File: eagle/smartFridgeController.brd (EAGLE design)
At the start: 35.9 x 41.9 mm, 13 parts

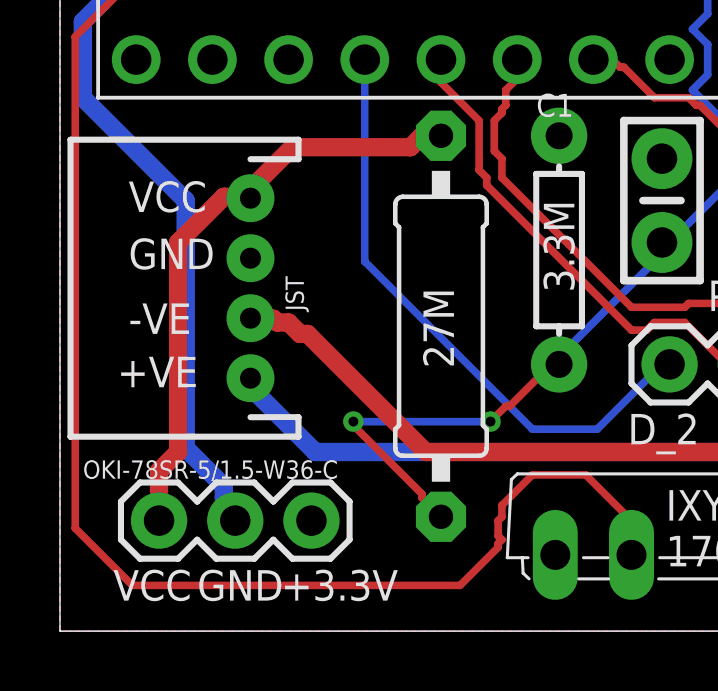
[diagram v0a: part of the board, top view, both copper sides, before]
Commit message: gnd, vcc switch, labled switch on oki-78
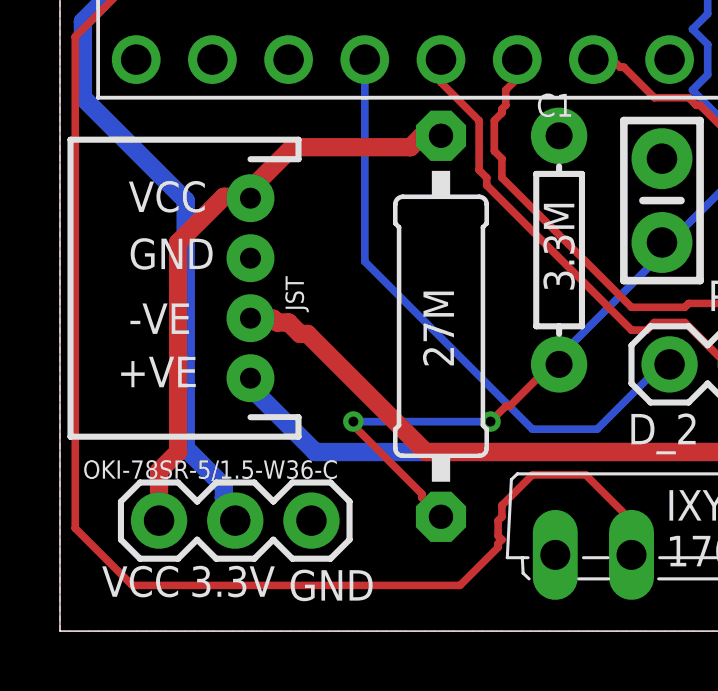
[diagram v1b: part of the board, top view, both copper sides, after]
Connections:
- new net N$4: JST.4
- net GND: no longer JST.3
- net VCC: now also JST.3; no longer JST.4
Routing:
- net VCC: track 20.0 -> 19.4 mm
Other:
- board text added: "3.3V"
- board text removed: "+3.3V"
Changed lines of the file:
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@@
 <text x="30.48" y="14.351" size="1.016" layer="25" font="vector" ratio="20">G_1</text>
 <text x="0.635" y="11.938" size="1.016" layer="25" font="vector" ratio="20">+VE</text>
-<text x="0.508" y="4.826" size="1.016" layer="25" font="vector" ratio="20">VCC</text>
-<text x="6.096" y="4.826" size="1.016" layer="25" font="vector" ratio="20">+3.3V</text>
-<text x="3.302" y="4.826" size="1.016" layer="25" font="vector" ratio="20">GND</text>
+<text x="0.127" y="4.953" size="1.016" layer="25" font="vector" ratio="20">VCC</text>
+<text x="3.048" y="4.953" size="1.016" layer="25" font="vector" ratio="20">3.3V</text>
+<text x="6.35" y="4.826" size="1.016" layer="25" font="vector" ratio="20">GND</text>
 <text x="14.605" y="20.955" size="0.762" layer="25" font="vector">C1</text>
 <text x="18.923" y="5.969" size="1.016" layer="25" font="vector" ratio="20">IXYS_CPC
@@
 <contactref element="C1" pad="2"/>
 <contactref element="R5" pad="P$1"/>
-<contactref element="JST" pad="3"/>
 <contactref element="OKI-78SR-5/1.5-W36-C" pad="3"/>
 <contactref element="18B20" pad="4"/>
@@
 <contactref element="IXYS_CPC_1706Y" pad="1"/>
 <contactref element="STATUS_LED" pad="2"/>
+<wire x1="31.75" y1="12.7" x2="31.75" y2="18.034" width="0" layer="19" extent="1-1"/>
+<wire x1="24.13" y1="12.7" x2="31.75" y2="12.7" width="0" layer="19" extent="1-1"/>
+<wire x1="18.796" y1="19.558" x2="24.13" y2="12.7" width="0" layer="19" extent="1-1"/>
+<wire x1="15.367" y1="20.32" x2="18.796" y2="19.558" width="0" layer="19" extent="1-1"/>
+<wire x1="15.24" y1="6.35" x2="24.13" y2="12.7" width="0" layer="19" extent="1-1"/>
+<wire x1="7.112" y1="7.493" x2="15.24" y2="6.35" width="0" layer="19" extent="1-1"/>
+<wire x1="1.27" y1="43.18" x2="15.367" y2="20.32" width="0" layer="19" extent="1-1"/>
 </signal>
 <signal name="VIN" class="1">
@@
 </signal>
 <signal name="VCC" class="1">
-<contactref element="JST" pad="4"/>
 <contactref element="R6" pad="2"/>
 <contactref element="OKI-78SR-5/1.5-W36-C" pad="1"/>
-<wire x1="5.08" y1="18.542" x2="5.08" y2="18.24" width="0.6096" layer="1"/>
 <wire x1="6.477" y1="19.939" x2="5.08" y2="18.542" width="0.6096" layer="1"/>
 <wire x1="10.414" y1="19.939" x2="6.477" y2="19.939" width="0.6096" layer="1"/>
@@
 <wire x1="4.191" y1="18.288" x2="2.667" y2="16.764" width="0.6096" layer="1"/>
 <wire x1="4.826" y1="18.288" x2="4.191" y2="18.288" width="0.6096" layer="1"/>
-<wire x1="4.826" y1="18.288" x2="5.08" y2="18.24" width="0.6096" layer="1"/>
+<contactref element="JST" pad="3"/>
+<wire x1="4.826" y1="18.288" x2="5.08" y2="18.542" width="0" layer="19" extent="1-1"/>
+<wire x1="5.08" y1="16.24" x2="4.826" y2="18.288" width="0" layer="19" extent="1-1"/>
 </signal>
 <signal name="+VE" class="1">
@@
 <wire x1="27.94" y1="36.957" x2="27.94" y2="37.592" width="0.254" layer="1"/>
 </signal>
+<signal name="N$4">
+<contactref element="JST" pad="4"/>
+</signal>
 </signals>

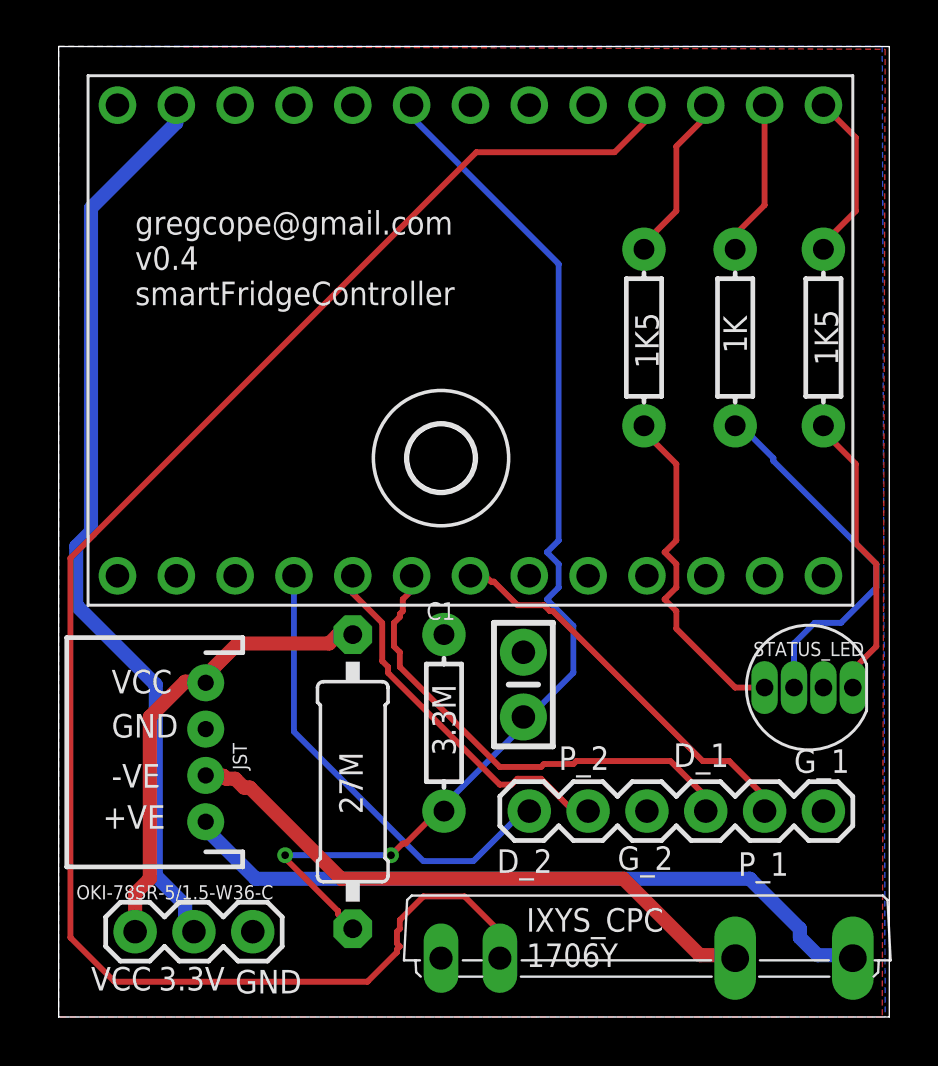
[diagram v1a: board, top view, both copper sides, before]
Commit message: silkscreen fixes, routing 0.3
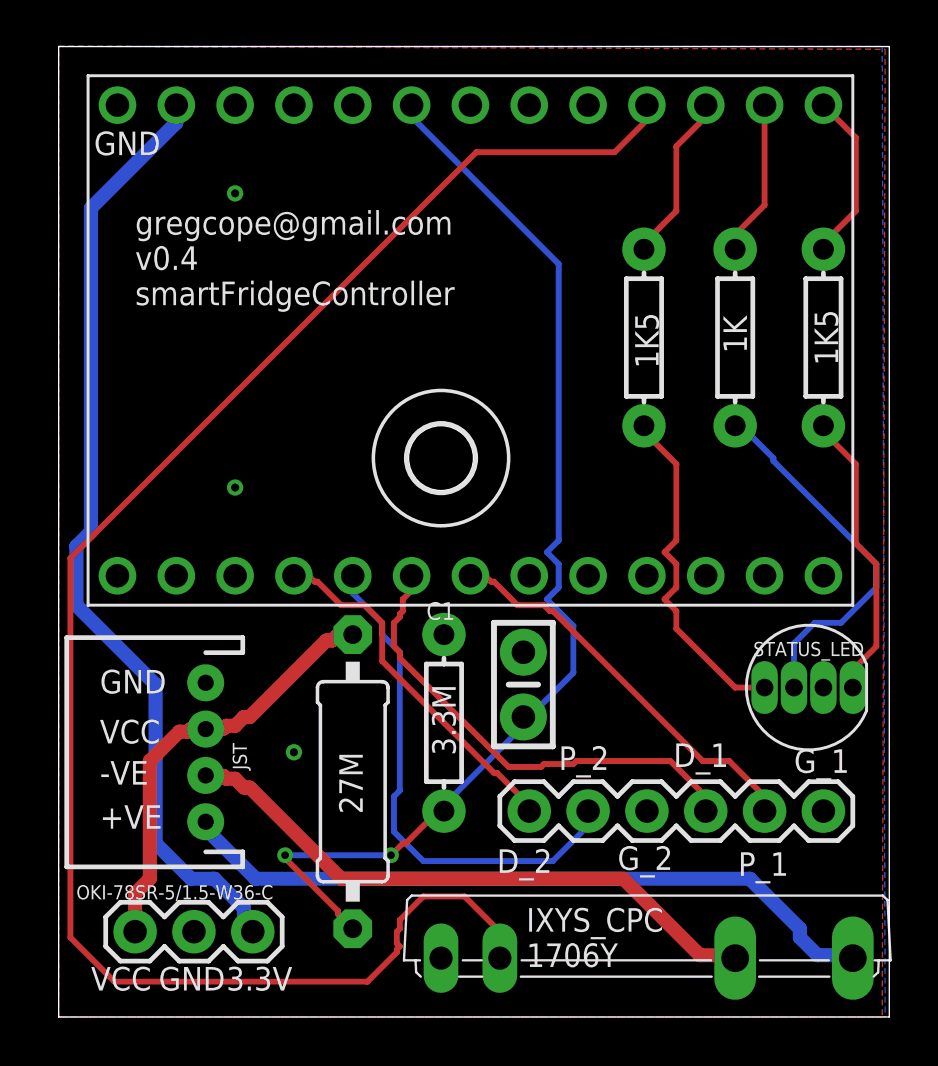
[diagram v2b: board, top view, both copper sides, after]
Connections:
- net GND: now also OKI-78SR-5/1.5-W36-C.2; no longer OKI-78SR-5/1.5-W36-C.3
- net VIN: now also OKI-78SR-5/1.5-W36-C.3; no longer OKI-78SR-5/1.5-W36-C.2
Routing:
- net D5_DS2_PWR: track 16.1 -> 22.2 mm
- net D4_DS2_DATA: track 20.1 -> 15.5 mm
- net VIN: track 39.6 -> 41.2 mm
- net VCC: track 19.4 -> 18.7 mm

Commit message: silkscreen updates
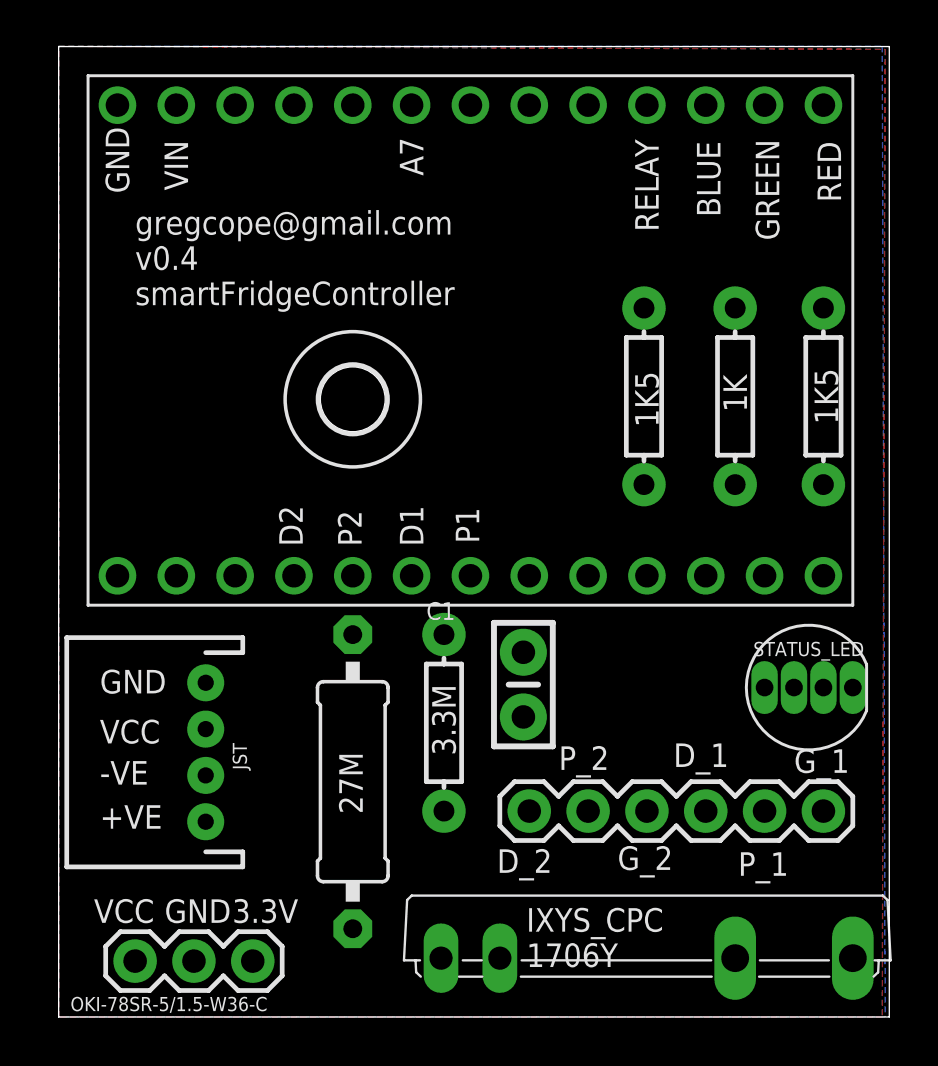
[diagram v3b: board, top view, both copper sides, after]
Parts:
- moved U$1 4.58 mm to (11.4, 30.5)
- moved R1 2.54 mm to (27.9, 30.6)
- moved R2 2.54 mm to (24.0, 30.6)
- moved R3 2.54 mm to (31.8, 30.6)
- moved OKI-78SR-5/1.5-W36-C 1.27 mm to (2.03, 6.22)
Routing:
- net D17_RELAY_PIN: track 73.2 -> 0.00 mm
- net A7_VCC_VD: track 48.7 -> 0.00 mm, vias 2 -> 0
- net VIN: track 41.2 -> 0.00 mm
- net +VE: track 30.8 -> 0.00 mm
- net -VE: track 26.1 -> 0.00 mm
- net D5_DS2_PWR: track 22.2 -> 0.00 mm
- net D6_DS1_DATA: track 20.5 -> 0.00 mm
- net VCC: track 18.7 -> 0.00 mm
- net D7_DS1_PWR: track 17.3 -> 0.00 mm
- net N$3: track 16.1 -> 0.00 mm
- net D4_DS2_DATA: track 15.5 -> 0.00 mm
- net N$2: track 15.0 -> 0.00 mm
- net N$1: track 12.7 -> 0.00 mm
- net D14_LED_RED_PIN: track 7.38 -> 0.00 mm
- net D16_LED_BLUE_PIN: track 7.33 -> 0.00 mm
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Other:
- board text added: "A7"
- board text added: "BLUE"
- board text added: "D1"
- board text added: "D2"
- board text added: "GREEN"
- board text added: "P1"
- board text added: "P2"
- board text added: "RED"
- board text added: "RELAY"
- board text added: "VIN"

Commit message: update
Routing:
- net D17_RELAY_PIN: track 0.00 -> 58.4 mm, vias 0 -> 1
- net A7_VCC_VD: track 0.00 -> 48.7 mm, vias 0 -> 2
- net VIN: track 0.00 -> 41.9 mm
- net +VE: track 0.00 -> 31.0 mm
- net -VE: track 0.00 -> 26.1 mm
- net D5_DS2_PWR: track 0.00 -> 22.2 mm
- net D6_DS1_DATA: track 0.00 -> 20.5 mm
- net VCC: track 0.00 -> 19.9 mm
- net D7_DS1_PWR: track 0.00 -> 17.3 mm
- net D4_DS2_DATA: track 0.00 -> 15.5 mm
- net N$2: track 0.00 -> 12.5 mm
- net N$3: track 0.00 -> 11.0 mm
- net N$1: track 0.00 -> 10.1 mm
- net D14_LED_RED_PIN: track 0.00 -> 9.92 mm
- net D16_LED_BLUE_PIN: track 0.00 -> 9.87 mm
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
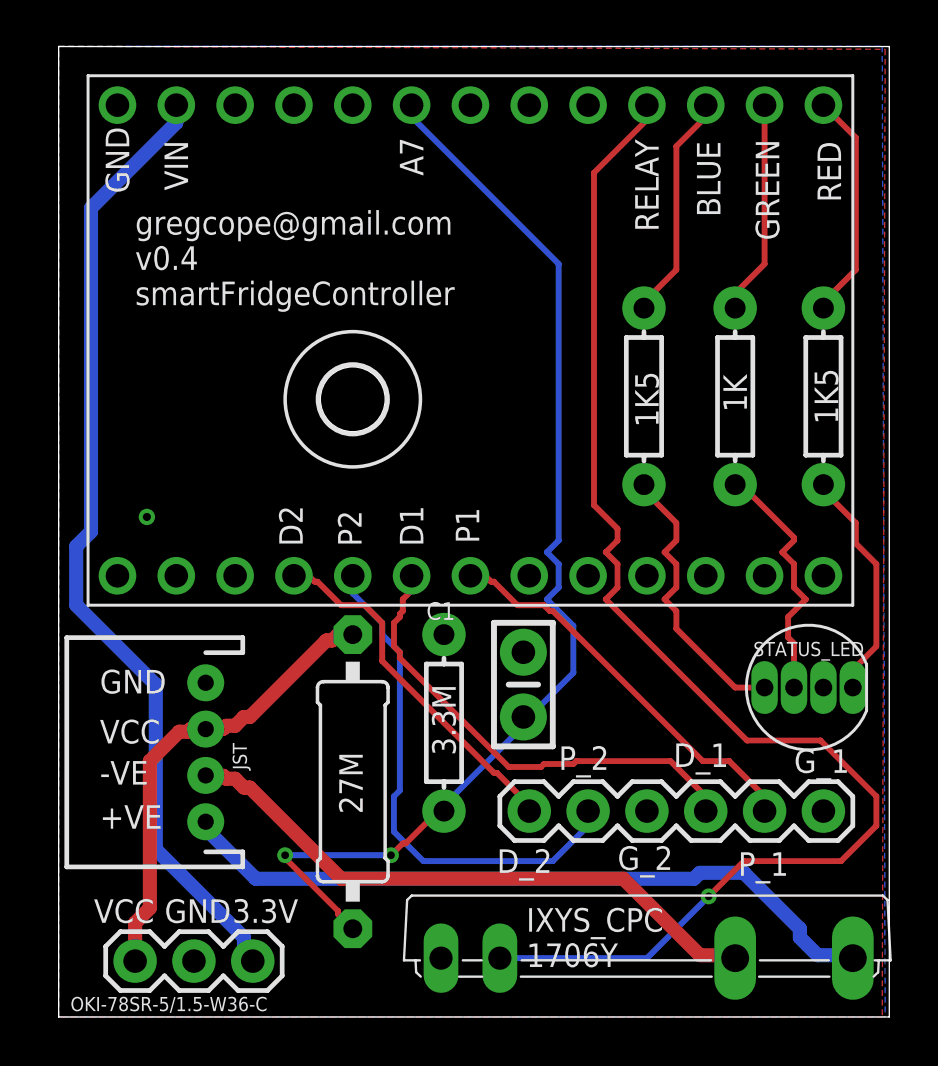
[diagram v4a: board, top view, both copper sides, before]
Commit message: Moved to screwterminal(s)
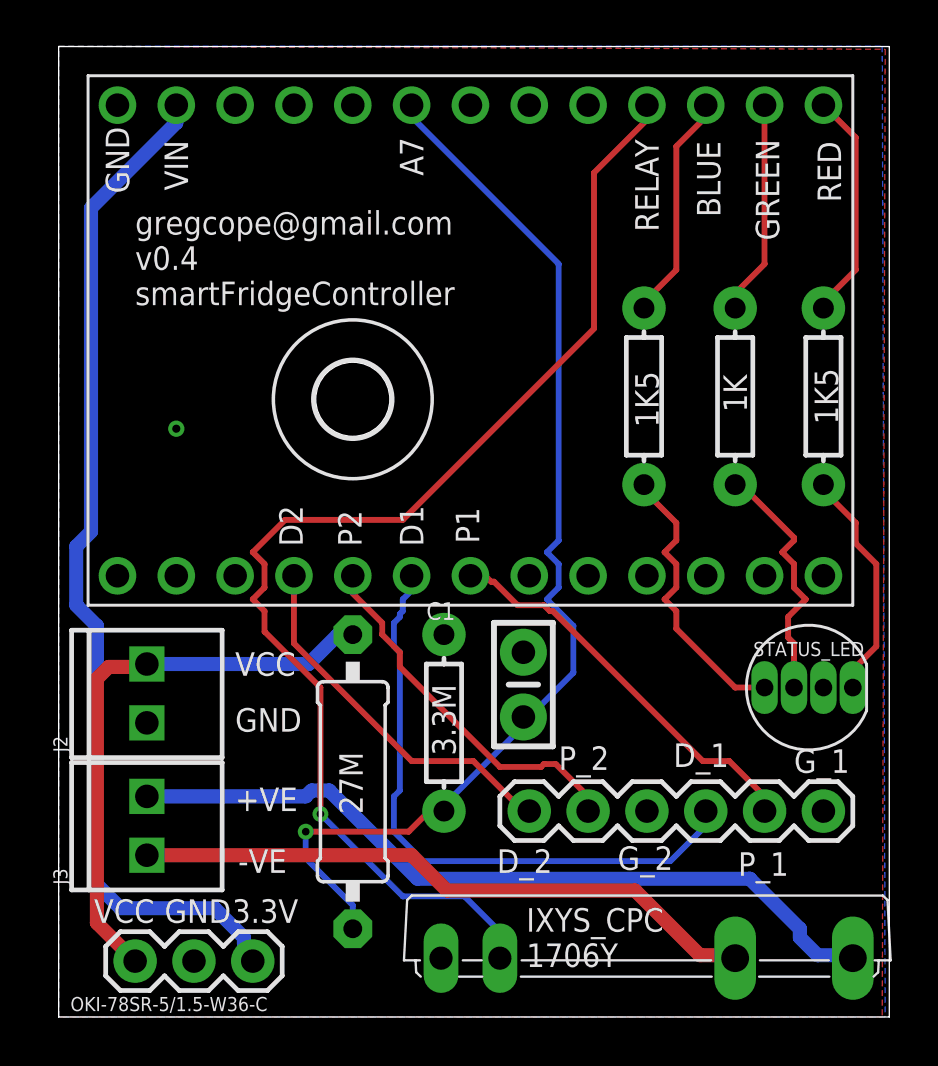
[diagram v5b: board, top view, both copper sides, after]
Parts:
- removed JST: 18B20, SparkFun-Connectors:JST-4-PTH
- removed U$1: (no value), holes:2,8
- added J2, J3: (no value), SparkFun-Connectors:1X02_2.54_SCREWTERM
- added U$3: (no value), holes:3,2
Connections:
- removed net N$4: JST.4
- net +VE: now also J3.P1; no longer JST.1
- net -VE: now also J3.P2; no longer JST.2
- net GND: now also J2.P2
- net VCC: now also J2.P1; no longer JST.3
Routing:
- net D6_DS1_DATA: track 20.5 -> 26.8 mm
- net D5_DS2_PWR: track 22.2 -> 16.0 mm
- net D17_RELAY_PIN: track 58.4 -> 53.3 mm
- net VCC: track 19.9 -> 24.7 mm
- net +VE: track 31.0 -> 33.8 mm
- net VIN: track 41.9 -> 44.3 mm
- net -VE: track 26.1 -> 27.2 mm
- net A7_VCC_VD: track 48.7 -> 48.0 mm, vias 2 -> 1
- net D4_DS2_DATA: track 15.5 -> 16.1 mm
